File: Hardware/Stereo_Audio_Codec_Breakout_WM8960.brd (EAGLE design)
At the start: 25.4 x 40.6 mm, 146 parts, among them J1 QWIIC, U3 XC6222B331MR-G, U4 WM8960, Y1 24 MHz

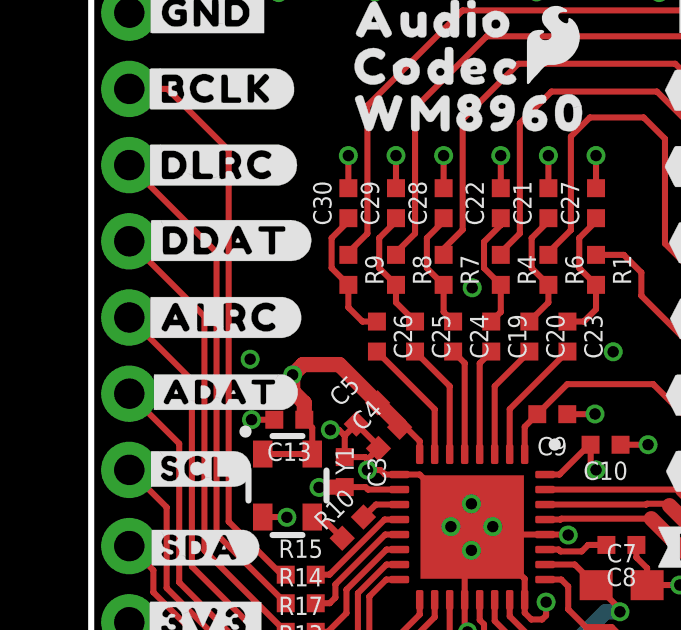
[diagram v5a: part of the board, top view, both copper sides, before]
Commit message: Corrected ADCDAT and DACDAT flag ends
ADCDAT will always be an output from the ADC.
DACDAT will always be an input - sent from the microcontroller that is sending SD to the DAC.
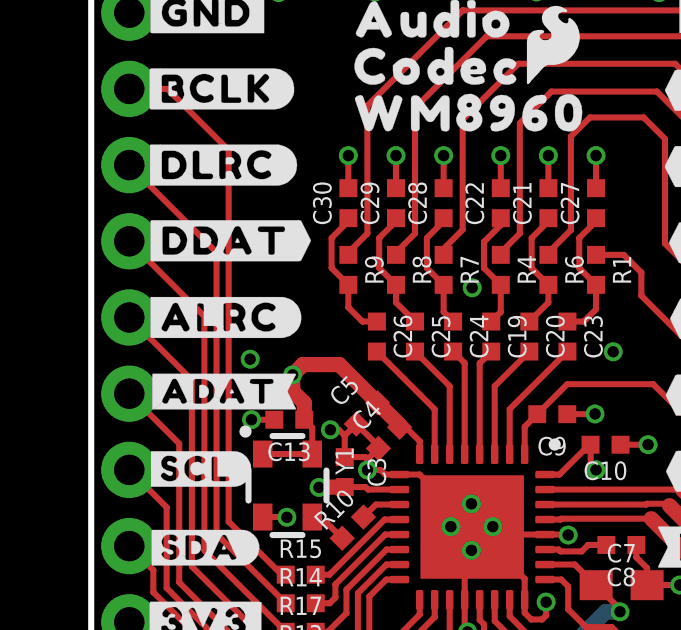
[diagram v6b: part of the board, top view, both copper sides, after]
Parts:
- removed U$25: (no value), output:#DDAT#2
- removed U$42: (no value), output:#ADAT#3
- removed U$43: (no value), output:#ADCDAT#1
- removed U$53: (no value), output:#DACDAT#3
- added U$58: (no value), output:#ADCDAT#6
- added U$69: (no value), output:#DDAT#9
- added U$70: (no value), output:#DACDAT#8
- added U$71: (no value), output:#ADAT#10
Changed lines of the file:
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@@
 <element name="U$23" library="output" package="#ALRC#0" value="" x="4.318" y="29.21" smashed="yes"/>
 <element name="U$24" library="output" package="#DLRC#1" value="" x="4.2418" y="34.29" smashed="yes"/>
-<element name="U$25" library="output" package="#DDAT#2" value="" x="4.4958" y="31.7754" smashed="yes"/>
-<element name="U$42" library="output" package="#ADAT#3" value="" x="4.3434" y="26.7208" smashed="yes"/>
-<element name="U$43" library="output" package="#ADCDAT#1" value="" x="5.6134" y="26.67" smashed="yes" rot="MR0"/>
 <element name="U$52" library="output" package="#ADCLRC#2" value="" x="5.3848" y="29.2354" smashed="yes" rot="MR0"/>
-<element name="U$53" library="output" package="#DACDAT#3" value="" x="5.6134" y="31.7754" smashed="yes" rot="MR0"/>
 <element name="U$55" library="output" package="#DACLRC#4" value="" x="5.3848" y="34.29" smashed="yes" rot="MR0"/>
 <element name="U$57" library="output" package="#BCLK#5" value="" x="4.2672" y="36.8554" smashed="yes" rot="MR0"/>
+<element name="U$58" library="output" package="#ADCDAT#6" value="" x="5.572759375" y="26.659840625" smashed="yes" rot="MR0"/>
+<element name="U$70" library="output" package="#DACDAT#8" value="" x="5.552440625" y="31.7347625" smashed="yes" rot="MR0"/>
+<element name="U$69" library="output" package="#DDAT#9" value="" x="4.4831" y="31.76778125" smashed="yes"/>
+<element name="U$71" library="output" package="#ADAT#10" value="" x="4.290059375" y="26.74111875" smashed="yes"/>
 </elements>
 <signals>
